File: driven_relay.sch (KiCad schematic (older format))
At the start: 4 parts, among them K1 301-1A-C-R1-U03-12VDC, Q5 NX138

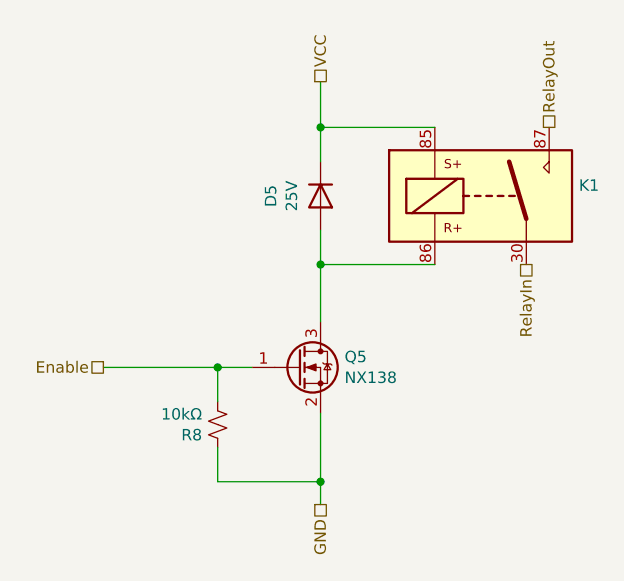
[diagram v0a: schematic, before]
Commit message: schematic update
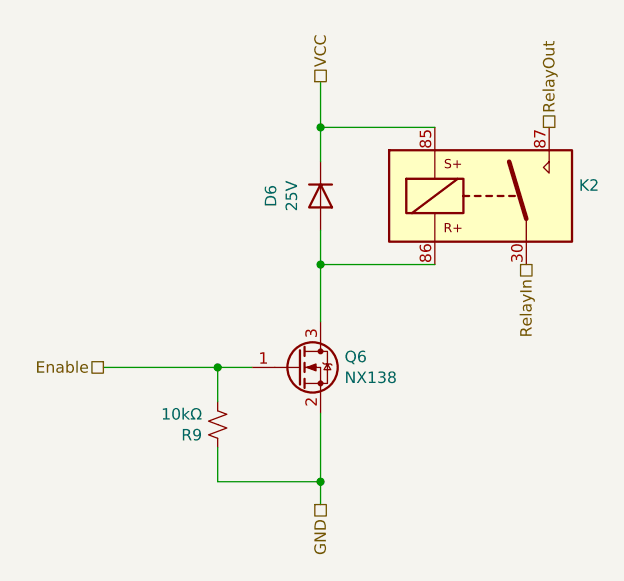
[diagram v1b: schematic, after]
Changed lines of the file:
@@
 $Descr A4 11693 8268
 encoding utf-8
-Sheet 7 9
+Sheet 8 9
 Title ""
 Date ""
@@
 AR Path="/619492C3/6194AD53" Ref="D5"  Part="1"
 AR Path="/619684B5/6194AD53" Ref="D6"  Part="1"
-F 0 "D5" H 4400 2333 50  0000 C CNN
+F 0 "D6" H 4400 2333 50  0000 C CNN
 F 1 "25V" H 4400 2424 50  0000 C CNN
 F 2 "Diode_SMD:D_SOT-23_ANK" H 4400 2550 50  0001 C CNN
@@
 AR Path="/619492C3/6194AD41" Ref="K1"  Part="1"
 AR Path="/619684B5/6194AD41" Ref="K2"  Part="1"
-F 0 "K1" H 5530 2596 50  0000 L CNN
+F 0 "K2" H 5530 2596 50  0000 L CNN
 F 1 "301-1A-C-R1-U03-12VDC" H 5530 2505 50  0001 L CNN
 F 2 "relays:Relay_1-Form-A_Song_Chuan-301-1A" H 5550 2500 50  0001 L CNN
@@
 AR Path="/619492C3/6194AD4D" Ref="R8"  Part="1"
 AR Path="/619684B5/6194AD4D" Ref="R9"  Part="1"
-F 0 "R8" H 4018 3596 50  0000 L CNN
+F 0 "R9" H 4018 3596 50  0000 L CNN
 F 1 "10kΩ" H 4018 3505 50  0000 L CNN
 F 2 "Resistor_SMD:R_0805_2012Metric" H 3950 3550 50  0001 C CNN
@@
 AR Path="/619492C3/6160D152" Ref="Q5"  Part="1"
 AR Path="/619684B5/6160D152" Ref="Q6"  Part="1"
-F 0 "Q5" H 4505 3346 50  0000 L CNN
+F 0 "Q6" H 4505 3346 50  0000 L CNN
 F 1 "NX138" H 4505 3255 50  0000 L CNN
 F 2 "Package_TO_SOT_SMD:SOT-23" H 4500 3225 50  0001 L CIN
